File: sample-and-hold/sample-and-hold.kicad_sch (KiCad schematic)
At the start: 11 parts, among them Q1 IRF3205, Q2 IRF3205, SW1 Trigger Button, U1 TL074

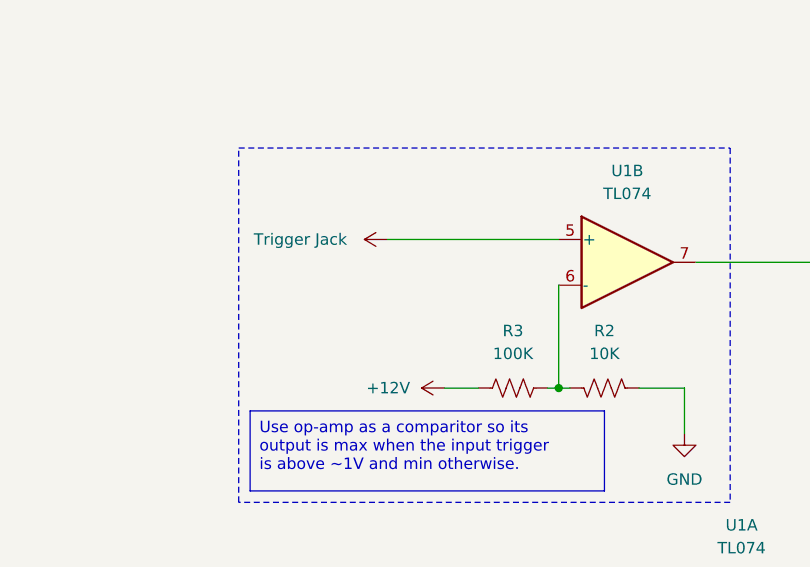
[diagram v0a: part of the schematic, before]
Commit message: Add a resistor to sample-and-hold
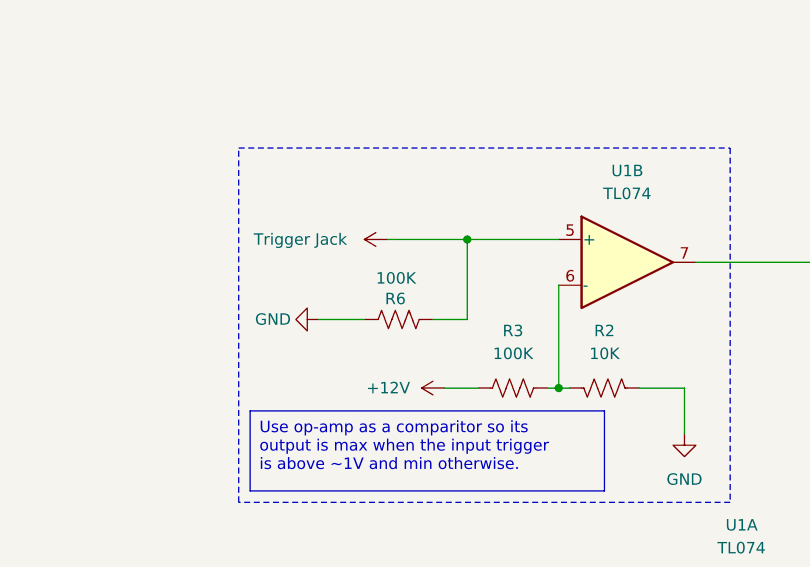
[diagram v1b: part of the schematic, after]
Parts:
- added R6: 100K, symbol Device:R_US
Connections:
- net GND: now also R6.1
- net Trigger Jack: now also R6.2
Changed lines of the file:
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@@
+	)
+	(junction
+		(at 87.63 66.04)
+		(diameter 0)
+		(color 0 0 0 0)
 	)
 	(junction
@@
 	(wire
 		(pts
+			(xy 83.82 74.93) (xy 87.63 74.93)
+		)
+		(stroke
+			(width 0)
+			(type default)
+		)
+	)
+	(wire
+		(pts
 			(xy 96.52 82.55) (xy 97.79 82.55)
 		)
@@
 	(wire
 		(pts
+			(xy 76.2 74.93) (xy 71.12 74.93)
+		)
+		(stroke
+			(width 0)
+			(type default)
+		)
+	)
+	(wire
+		(pts
 			(xy 170.18 68.58) (xy 173.99 68.58)
 		)
@@
 	(wire
 		(pts
+			(xy 87.63 74.93) (xy 87.63 66.04)
+		)
+		(stroke
+			(width 0)
+			(type default)
+		)
+	)
+	(wire
+		(pts
 			(xy 149.86 100.33) (xy 142.24 100.33)
 		)
@@
 	(wire
 		(pts
-			(xy 78.74 66.04) (xy 97.79 66.04)
+			(xy 78.74 66.04) (xy 87.63 66.04)
 		)
 		(stroke
@@
 		(pts
 			(xy 125.73 107.95) (xy 137.16 107.95)
+		)
+		(stroke
+			(width 0)
+			(type default)
+		)
+	)
+	(wire
+		(pts
+			(xy 87.63 66.04) (xy 97.79 66.04)
 		)
 		(stroke
@@
 	)
 	(symbol
+		(lib_id "power:GND")
+		(at 71.12 74.93 270)
+		(unit 1)
+		(exclude_from_sim no)
+		(in_bom yes)
+		(on_board yes)
+		(dnp no)
+		(property "Reference" "#PWR012"
+			(at 64.77 74.93 0)
+			(effects
+				(font
+					(size 1.27 1.27)
+				)
+				(hide yes)
+			)
+		)
+		(property "Value" "GND"
+			(at 66.04 74.93 90)
+			(effects
+				(font
+					(size 1.27 1.27)
+				)
+			)
+		)
+		(property "Footprint" ""
+			(at 71.12 74.93 0)
+			(effects
+				(font
+					(size 1.27 1.27)
+				)
+				(hide yes)
+			)
+		)
+		(property "Datasheet" ""
+			(at 71.12 74.93 0)
+			(effects
+				(font
+					(size 1.27 1.27)
+				)
+				(hide yes)
+			)
+		)
+		(property "Description" "Power symbol creates a global label with name \"GND\" , ground"
+			(at 71.12 74.93 0)
+			(effects
+				(font
+					(size 1.27 1.27)
+				)
+				(hide yes)
+			)
+		)
+		(pin "1"
+		)
+		(instances
+			(project "sample-and-hold"
+				(path "/767d3279-7c6d-4a44-94c9-b23c47779f48"
+					(reference "#PWR012")
+					(unit 1)
+				)
+			)
+		)
+	)
+	(symbol
 		(lib_id "Amplifier_Operational:TL074")
 		(at 33.02 34.29 90)
@@
 				)
 			)
+		)
+	)
+	(symbol
+		(lib_id "Device:R_US")
+		(at 80.01 74.93 90)
+		(unit 1)
+		(exclude_from_sim no)
+		(in_bom yes)
+		(on_board yes)
+		(dnp no)
+		(property "Reference" "R6"
+			(at 78.486 72.644 90)
+			(effects
+				(font
+					(size 1.27 1.27)
+				)
+				(justify right)
+			)
+		)
+		(property "Value" "100K"
+			(at 77.47 70.358 90)
+			(effects
+				(font
+					(size 1.27 1.27)
+				)
+				(justify right)
+			)
+		)
+		(property "Footprint" ""
+			(at 80.264 73.914 90)
+			(effects
+				(font
+					(size 1.27 1.27)
+				)
+				(hide yes)
+			)
+		)
+		(property "Datasheet" "~"
+			(at 80.01 74.93 0)
+			(effects
+				(font
+					(size 1.27 1.27)
+				)
+				(hide yes)
+			)
+		)
+		(property "Description" "Resistor, US symbol"
+			(at 80.01 74.93 0)
+			(effects
+				(font
+					(size 1.27 1.27)
+				)
+				(hide yes)
+			)
+		)
+		(pin "2"
+		)
+		(pin "1"
+		)
+		(instances
+			(project "sample-and-hold"
+				(path "/767d3279-7c6d-4a44-94c9-b23c47779f48"
+					(reference "R6")
+					(unit 1)
+				)
+			)
